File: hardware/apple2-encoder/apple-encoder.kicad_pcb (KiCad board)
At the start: 2 copper layers, 88.9 x 132.1 mm, 50 parts, among them J1 Apple 2, J10 Keyboard, J2 Apple 1, J3 UART, J4 Conn_01x05, J5 SOL-20, J6 Programming, J7 Custom Connector 1 / Proto, J8 Apple II+ matrix, SW1 Options, U1 ATmega2560-16AU, Y1 16.000 MHz

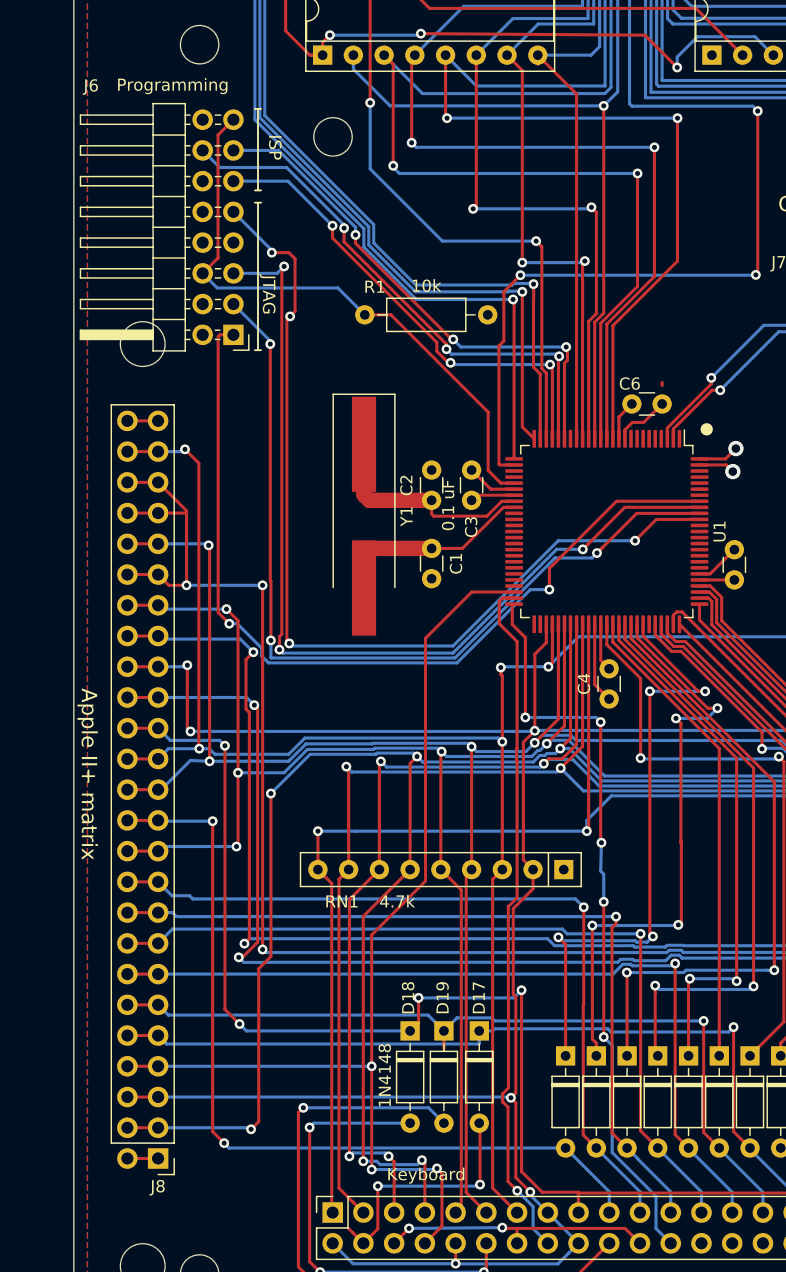
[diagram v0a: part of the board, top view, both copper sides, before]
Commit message: Fixed Keyboard encoder connector
- remove unused "jumper holes"
- align pins with spacer holes.
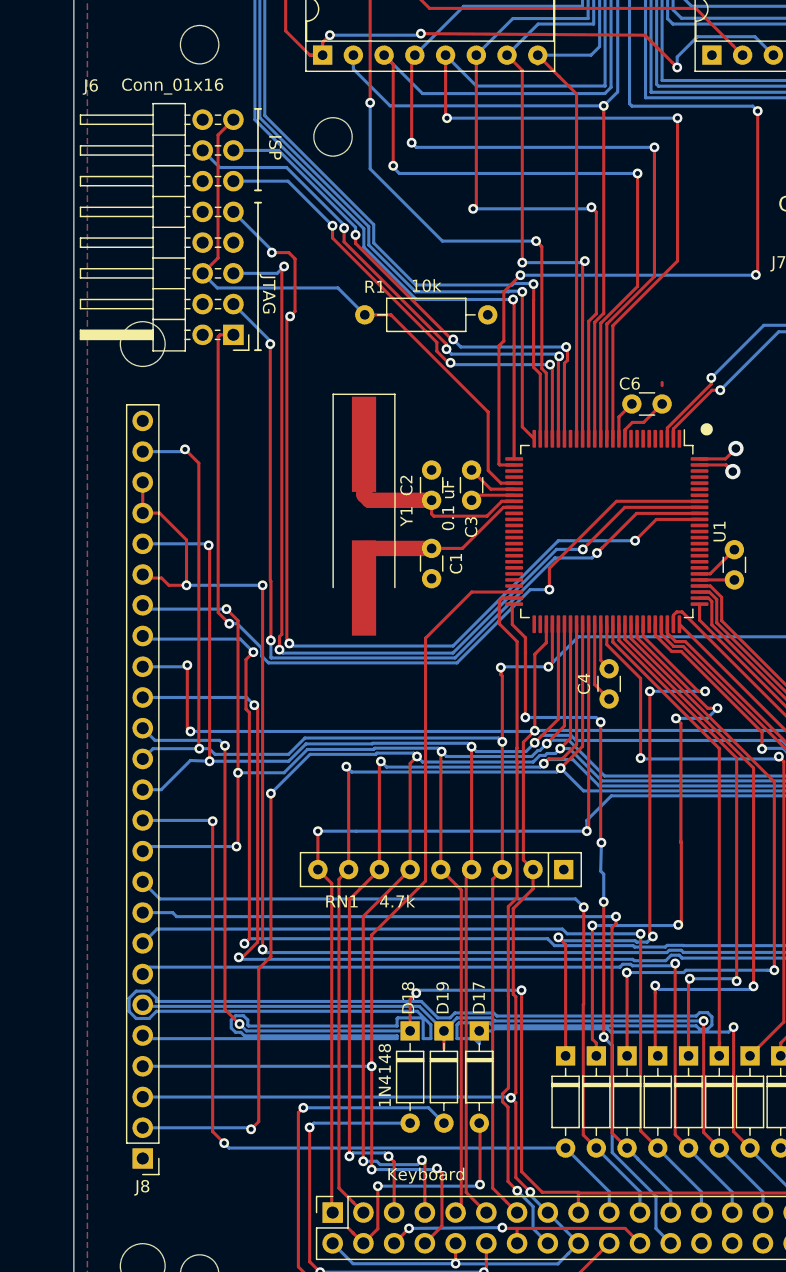
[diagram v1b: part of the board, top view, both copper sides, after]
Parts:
- J6: value Programming -> Conn_01x16
- J8: value Apple II+ matrix -> Conn_01x25; footprint unikbd:ExpansionHeader_1x25_P2.54 -> Connector_PinHeader_2.54mm:PinHeader_1x25_P2.54mm_Vertical
- moved J8 1.27 mm to (169.5, 168.6)
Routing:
- net /Row0: track 67.1 -> 199.3 mm
- net /Col3: track 152.9 -> 155.6 mm
- net /Col2: track 141.4 -> 143.9 mm
- net /Col1: track 139.7 -> 142.3 mm
- net /Col0: track 171.7 -> 174.2 mm
- net /Row7: track 115.7 -> 117.3 mm
- net /Col4: track 166.4 -> 167.7 mm
- net /Row6: track 66.8 -> 68.0 mm
- net /Row5: track 63.2 -> 64.5 mm
- net /Row4: track 64.5 -> 65.8 mm
- net /Row3: track 65.6 -> 66.8 mm
- net /Row2: track 65.7 -> 66.9 mm
- net /Row1: track 65.8 -> 67.0 mm
- net /LED1: track 84.7 -> 85.9 mm
- net /Row10: track 121.0 -> 122.3 mm
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
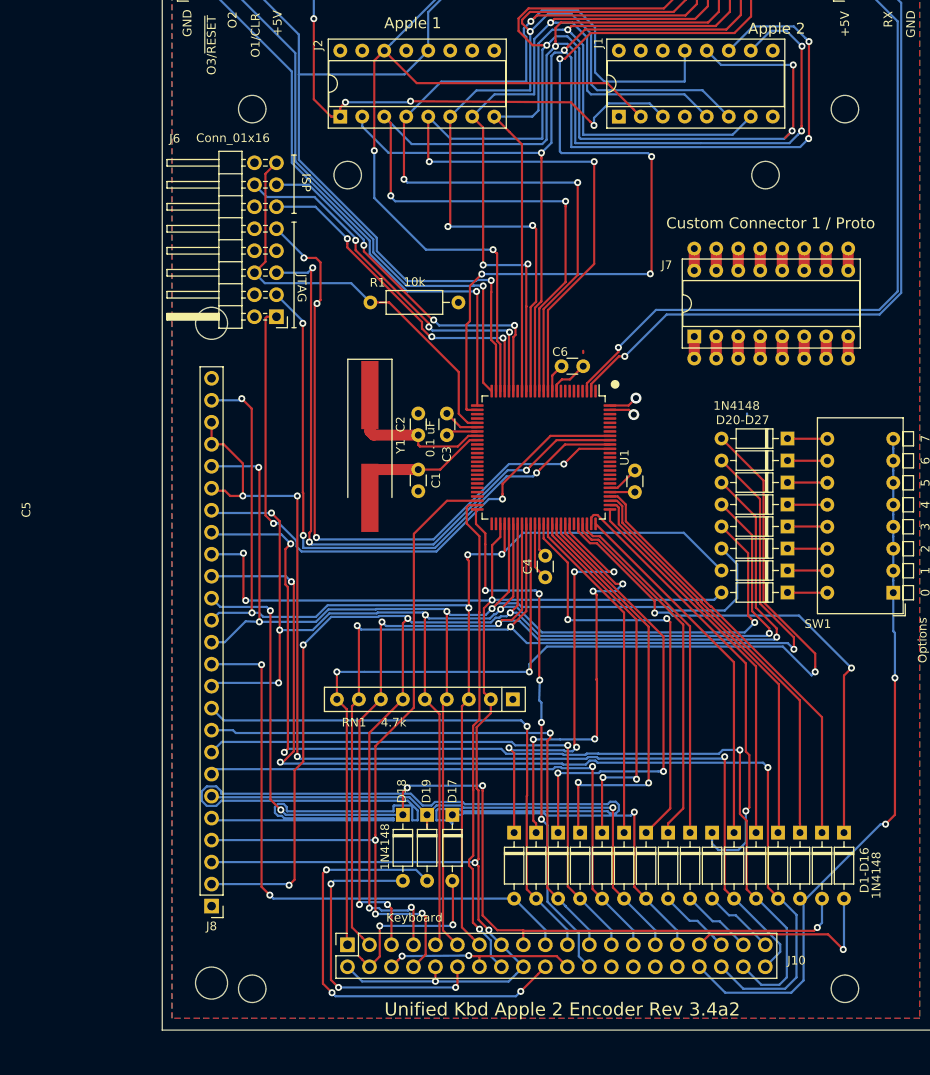
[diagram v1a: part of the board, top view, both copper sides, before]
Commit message: Convert the Apple II encoder to all-SMT parts (except connectors).
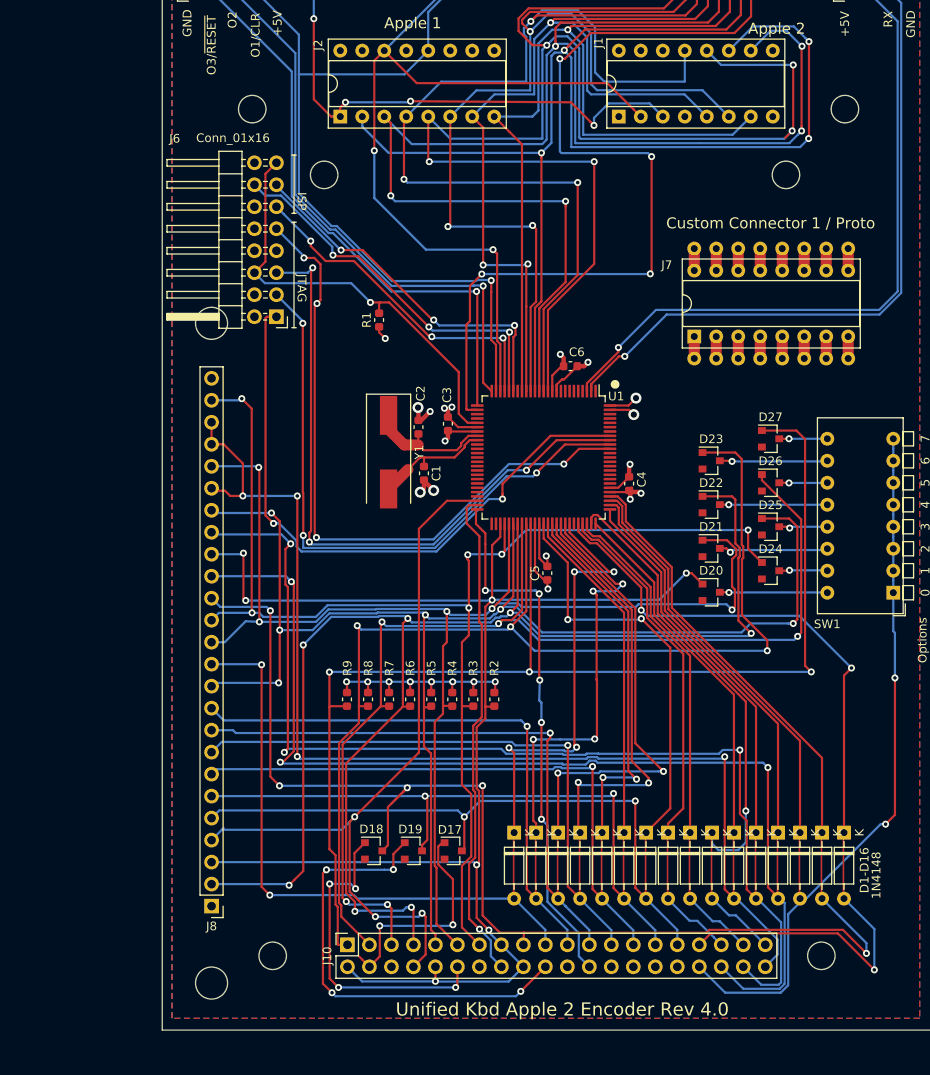
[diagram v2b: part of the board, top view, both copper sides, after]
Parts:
- removed RN1: 4.7k, Resistor_THT:R_Array_SIP9
- added R2: 10k, Resistor_SMD:R_0603_1608Metric, F.Cu at (202.2, 144.7)
- added R3: 10k, Resistor_SMD:R_0603_1608Metric, F.Cu at (199.8, 144.7)
- added R4: 10k, Resistor_SMD:R_0603_1608Metric, F.Cu at (197.3, 144.7)
- added R5: 10k, Resistor_SMD:R_0603_1608Metric, F.Cu at (194.9, 144.7)
- added R6: 10k, Resistor_SMD:R_0603_1608Metric, F.Cu at (192.5, 144.7)
- added R7: 10k, Resistor_SMD:R_0603_1608Metric, F.Cu at (190.0, 144.7)
- added R8: 10k, Resistor_SMD:R_0603_1608Metric, F.Cu at (187.6, 144.7)
- added R9: 10k, Resistor_SMD:R_0603_1608Metric, F.Cu at (185.2, 144.7)
- C1, C2, C3, C4, C5, C6: footprint Capacitor_THT:C_Disc_D3.0mm_W1.6mm_P2.50mm -> Capacitor_SMD:C_0603_1608Metric
- D1, D10, D11, D12, D13, D14, D15, D16, D2, D3, D4, D5, D6, D7, D8, D9: footprint Diode_THT:D_DO-35_SOD27_P7.62mm_Horizontal -> unikbd:D_DO-35_SOD27_P7.62mm_Horizontal_bypassed
- D17, D18, D19, D20, D21, D22, D23, D24, D25, D26, D27: footprint Diode_THT:D_DO-35_SOD27_P7.62mm_Horizontal -> Diode_SMD:D_SOT-23_ANK
- J10: footprint unikbd:PinHeader_2x20_P2.54mm_Vertical -> unikbd:kbd_header_and_mounting_holes
- R1: footprint Resistor_THT:R_Axial_DIN0207_L6.3mm_D2.5mm_P10.16mm_Horizontal -> Resistor_SMD:R_0603_1608Metric
- Y1: footprint Crystal:Crystal_SMD_HC49-SD_HandSoldering -> Crystal:Crystal_SMD_HC49-SD
- moved C4 14.5 mm to (217.8, 119.8)
- moved C5 13.8 mm to (208.3, 130.1)
- moved R1 9.38 mm to (188.9, 100.9), turned to 90 degrees
- moved D20 8.81 mm to (227.2, 132.3), turned to 0 degrees
- moved D23 8.81 mm to (227.2, 117.1), turned to 0 degrees
- moved D21 8.81 mm to (227.2, 127.2), turned to 0 degrees
- moved D22 8.81 mm to (227.2, 122.2), turned to 0 degrees
- moved D18 5.36 mm to (188.2, 162.2), turned to 0 degrees
- moved D19 4.45 mm to (192.8, 162.2), turned to 0 degrees
- moved D17 4.17 mm to (197.4, 162.2), turned to 0 degrees
- moved Y1 2.25 mm to (190.0, 116.1)
- moved D25 1.96 mm to (234.1, 124.7), turned to 0 degrees
- moved D26 1.96 mm to (234.1, 119.7), turned to 0 degrees
- moved D27 1.96 mm to (234.1, 114.6), turned to 0 degrees
- moved D24 1.96 mm to (234.1, 129.8), turned to 0 degrees
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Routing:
- net /Row0: track 199.3 -> 73.1 mm, vias 1 -> 2
- net /Row7: track 117.3 -> 134.8 mm
- net VCC: track 44.8 -> 57.9 mm, vias 3 -> 16
- net GND: track 20.2 -> 32.5 mm, vias 1 -> 9
- net /Row15: track 23.8 -> 32.2 mm
- net /Col3: track 155.6 -> 163.7 mm
- net Net-(D21-Pad1): track 4.61 -> 12.8 mm, vias 0 -> 1
- net /Col1: track 142.3 -> 150.3 mm, vias 5 -> 6
- net Net-(D23-Pad1): track 4.61 -> 12.5 mm, vias 0 -> 1
- net Net-(D20-Pad1): track 4.61 -> 12.4 mm, vias 0 -> 1
- net Net-(D22-Pad1): track 4.61 -> 12.4 mm, vias 0 -> 1
- net /Col2: track 143.9 -> 150.2 mm, vias 4 -> 5
- net /Col5: track 122.9 -> 128.7 mm
- net /Row1: track 67.0 -> 72.6 mm, vias 1 -> 2
- net Net-(D17-Pad2): track 20.5 -> 26.1 mm
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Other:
- outline, holes or cut-outs redrawn
- board text added: "Unified Kbd Apple 2 Encoder Rev 4.0"
- board text removed: "D20-D27"
- board text removed: "Mounting holes: 0.125" Non-plated 2.5" square spacing Pin 1 of connector 0.31", 0" (x,y) relative to center of left lower hole."
- board text removed: "Pin 1 of keyboard connector must be at least 3.5" from pin 1 of interface connector in order for interface connector to be accessible with keyboard assembled."
- board text removed: "Unified Kbd Apple 2 Encoder Rev 3.4a2"

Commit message: Add BOM parameter fields to apple2 and 328P encoders and classic kbd
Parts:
- J4: value Conn_01x05 -> Outputs
- J6: value Conn_01x16 -> Programming
- J8: value Conn_01x25 -> Apple II Matrix

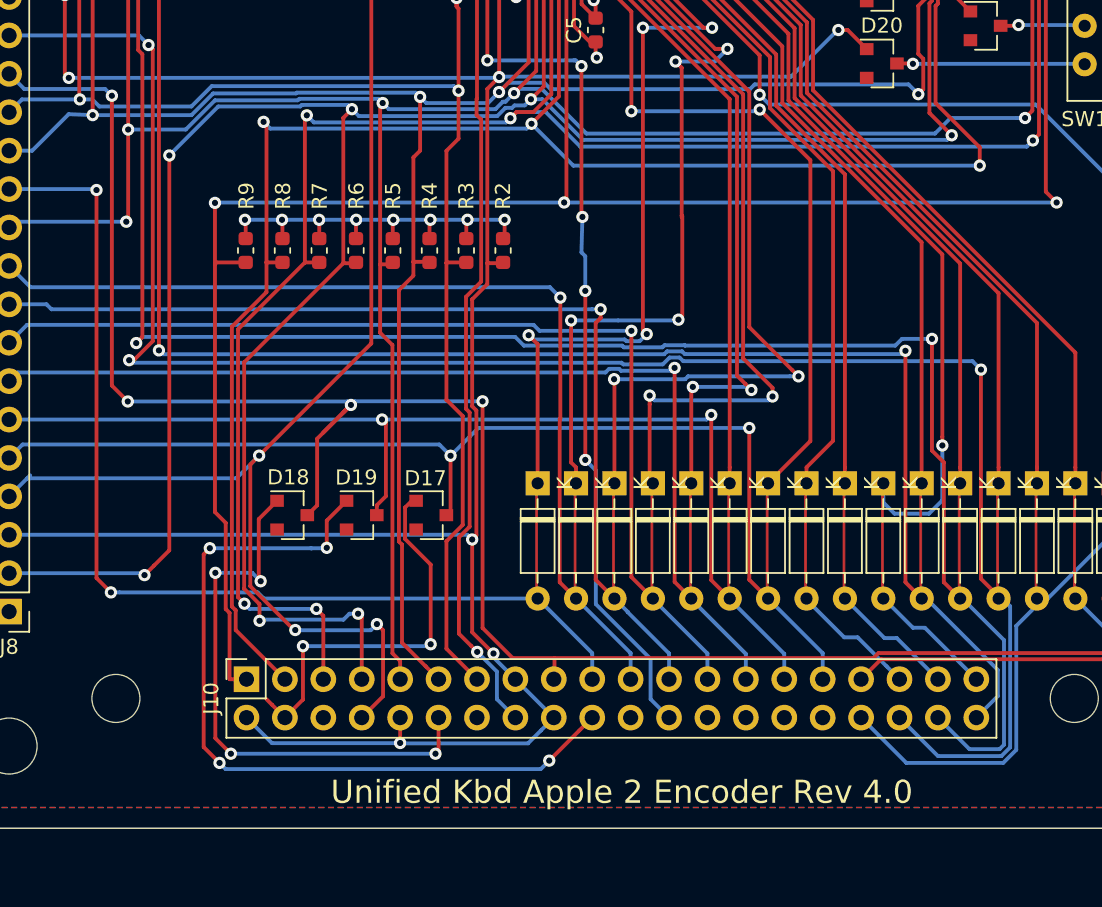
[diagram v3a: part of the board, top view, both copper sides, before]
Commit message: Remove unneeded pullups from Atmega2560 smt encoder
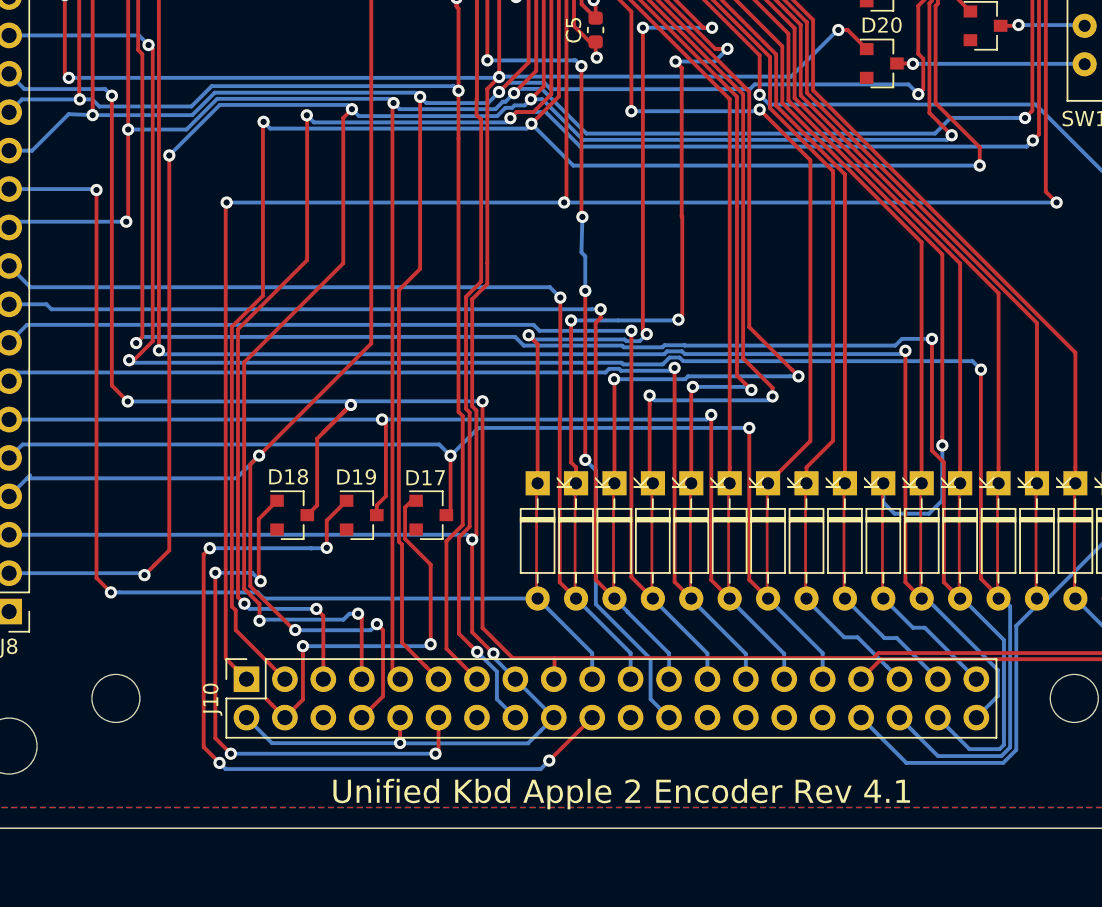
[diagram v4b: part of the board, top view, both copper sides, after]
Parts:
- removed R2, R3, R4, R5, R6, R7, R8, R9: 10k, Resistor_SMD:R_0603_1608Metric
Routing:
- net VCC: track 57.9 -> 30.7 mm, vias 16 -> 8
- net /Col7: track 140.5 -> 136.8 mm
- net /Col1: track 150.3 -> 148.3 mm
- net /Col3: track 163.7 -> 162.5 mm
- net /Col6: track 130.2 -> 129.0 mm
- net /Col2: track 150.2 -> 149.1 mm
- net /Col0: track 174.1 -> 173.1 mm
- net /Col5: track 128.7 -> 127.8 mm
- net /Col4: track 173.1 -> 172.2 mm
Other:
- board text added: "Unified Kbd Apple 2 Encoder Rev 4.1"
- board text removed: "Unified Kbd Apple 2 Encoder Rev 4.0"

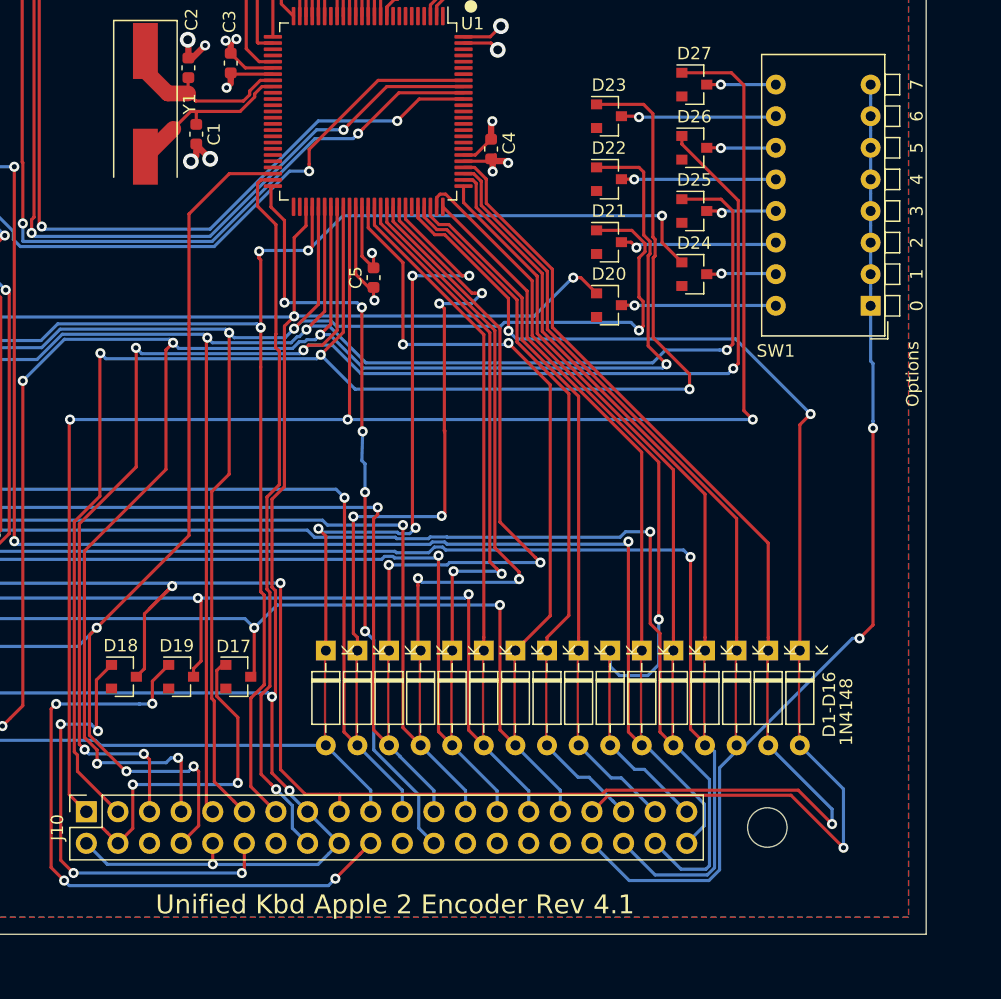
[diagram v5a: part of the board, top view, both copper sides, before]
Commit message: Modify to use DIP switch or jumpers
- Add combined DIP-switch/Jumper footprint to footprint library
- Fix Apple2-encoder and interface-ascii-atmega2560 schematics and PCB to use
new footprint.
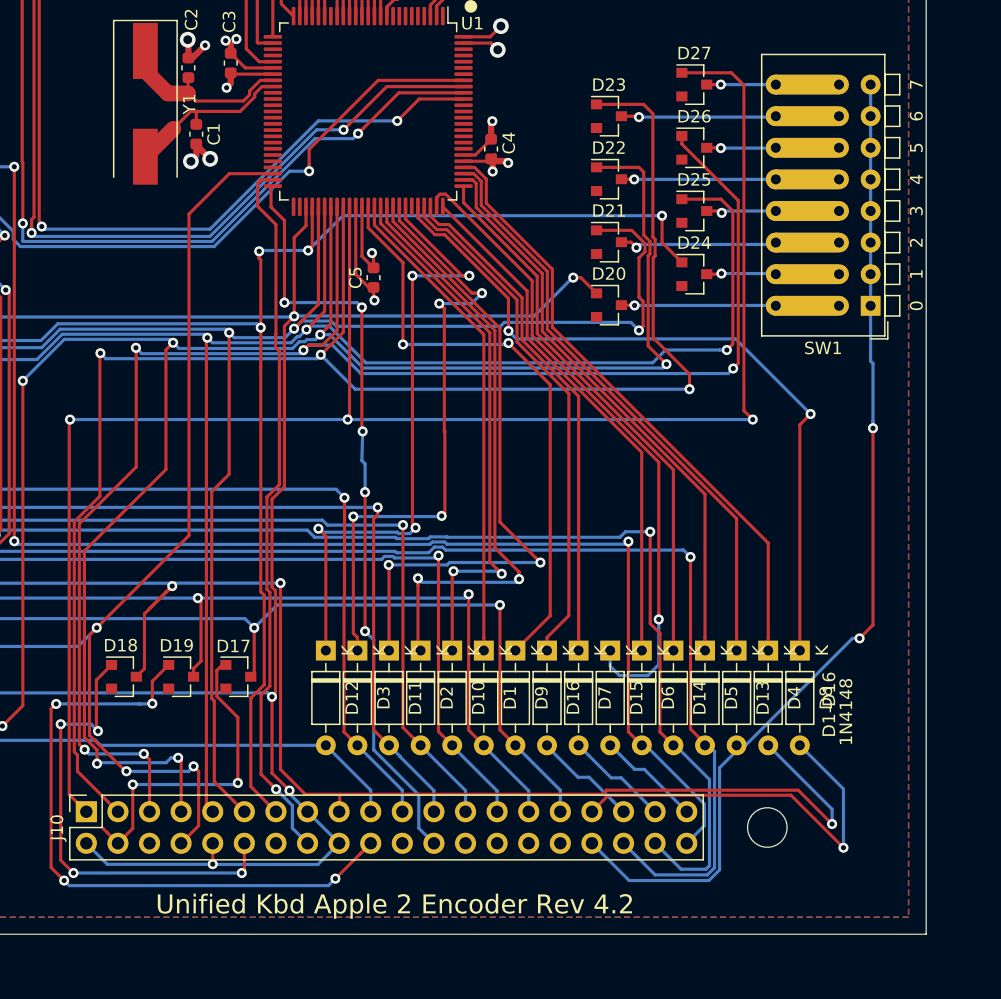
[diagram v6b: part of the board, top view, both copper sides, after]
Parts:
- D1, D10, D11, D12, D13, D14, D15, D16, D2, D3, D4, D5, D6, D7, D8, D9: footprint unikbd:D_DO-35_SOD27_P7.62mm_Horizontal_bypassed -> Diode_THT:D_DO-35_SOD27_P7.62mm_Horizontal
- SW1: footprint Button_Switch_THT:SW_DIP_SPSTx08_Piano_CTS_Series194-8MSTN_W7.62mm_P2.54mm -> unikbd:SW_DIP_SPSTx08_Piano_CTS_Series194-8MSTN_W7.62mm_P2.54mm
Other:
- board text added: "Unified Kbd Apple 2 Encoder Rev 4.2"
- board text removed: "Unified Kbd Apple 2 Encoder Rev 4.1"
